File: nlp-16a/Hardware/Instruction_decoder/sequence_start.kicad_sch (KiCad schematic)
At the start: 6 parts, among them U35 State_hold_unit, U36 State_hold_unit, U63 CD74HC00, U64 CD74HC00, U83 CD74HC00, U84 CD74HC00

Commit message: 基板設計 今日はとりあえずここまで
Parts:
- U35, U36: footprint (none) -> Connector_PinSocket_2.54mm:PinSocket_1x05_P2.54mm_Vertical
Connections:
- net ~{SP_DEC_INT1->}: now also U83.2; no longer U83.1
- net at U84.6: now also U83.1; no longer U83.2
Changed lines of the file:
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@@
     (property "Reference" "U35" (id 0) (at 121.92 88.9 0))
     (property "Value" "State_hold_unit" (id 1) (at 121.92 91.44 0))
-    (property "Footprint" "" (id 2) (at 121.92 92.71 0)
+    (property "Footprint" "Connector_PinSocket_2.54mm:PinSocket_1x05_P2.54mm_Vertical" (id 2) (at 121.92 92.71 0)
       (effects (font (size 1.27 1.27)) hide)
     )
@@
     (property "Reference" "U36" (id 0) (at 153.67 88.9 0))
     (property "Value" "State_hold_unit" (id 1) (at 153.67 91.44 0))
-    (property "Footprint" "" (id 2) (at 153.67 92.71 0)
+    (property "Footprint" "Connector_PinSocket_2.54mm:PinSocket_1x05_P2.54mm_Vertical" (id 2) (at 153.67 92.71 0)
       (effects (font (size 1.27 1.27)) hide)
     )
@@
     (pin "13")
   )
-  (symbol (lib_id "CD74HCXX:CD74HC00") (at 130.81 132.08 0) (mirror x) (unit 1)
+  (symbol (lib_id "CD74HCXX:CD74HC00") (at 130.81 132.08 0) (unit 1)
     (in_bom yes) (on_board yes)
     (property "Reference" "U83" (id 0) (at 130.81 123.19 0))
     (property "Value" "CD74HC00" (id 1) (at 130.81 125.73 0))
-    (property "Footprint" "Package_DIP:DIP-14_W7.62mm" (id 2) (at 130.81 138.43 0)
-      (effects (font (size 1.27 1.27)) hide)
-    )
+    (property "Footprint" "Package_DIP:DIP-14_W7.62mm" (id 2) (at 130.81 125.73 0)
+      (effects (font (size 1.27 1.27)) hide)
+    )

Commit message: 基板設計 進捗
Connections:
- net at U63.4: now also U63.3; no longer U36.5 (~{Q})
- net at U63.5: now also U36.5 (~{Q}); no longer U63.3
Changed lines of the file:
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@@
     (pin "13")
   )
-  (symbol (lib_id "CD74HCXX:CD74HC00") (at 173.99 87.63 0) (mirror x) (unit 2)
+  (symbol (lib_id "CD74HCXX:CD74HC00") (at 173.99 87.63 0) (unit 2)
     (in_bom yes) (on_board yes)
-    (property "Reference" "U63" (id 0) (at 173.99 78.74 0))
-    (property "Value" "CD74HC00" (id 1) (at 173.99 81.28 0))
-    (property "Footprint" "Package_DIP:DIP-14_W7.62mm" (id 2) (at 173.99 93.98 0)
+    (property "Reference" "U63" (id 0) (at 173.99 80.01 0))
+    (property "Value" "CD74HC00" (id 1) (at 173.99 82.55 0))
+    (property "Footprint" "Package_DIP:DIP-14_W7.62mm" (id 2) (at 173.99 81.28 0)
       (effects (font (size 1.27 1.27)) hide)
     )

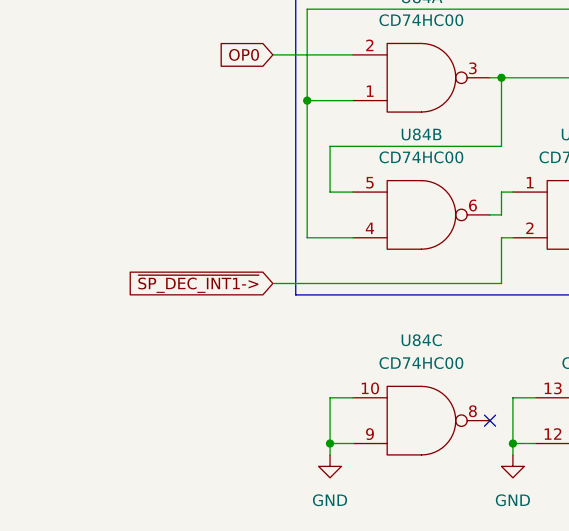
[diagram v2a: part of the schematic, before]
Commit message: 命令デコーダ修正
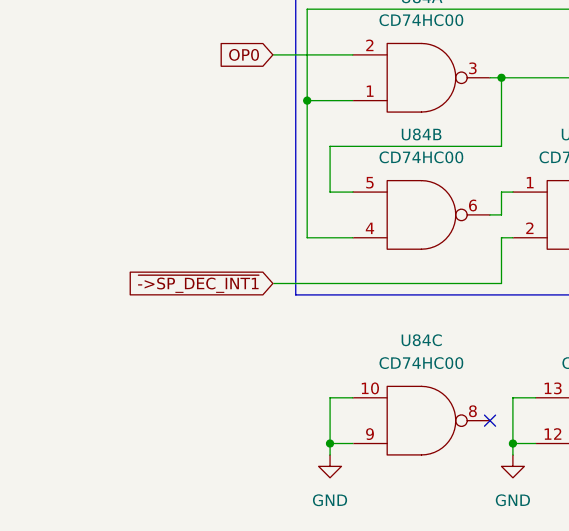
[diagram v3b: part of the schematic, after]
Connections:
- net ~{SP_DEC_INT1->} renamed ~{->SP_DEC_INT1}
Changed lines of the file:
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@@
     )
   )
-  (global_label "~{SP_DEC_INT1->}" (shape input) (at 96.52 139.7 180) (fields_autoplaced)
+  (global_label "~{->SP_DEC_INT1}" (shape input) (at 96.52 139.7 180) (fields_autoplaced)
     (effects (font (size 1.27 1.27)) (justify right))
     (property "Intersheet References" "${INTERSHEET_REFS}" (id 0) (at 78.7459 139.6206 0)
